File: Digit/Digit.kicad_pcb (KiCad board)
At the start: 2 copper layers, 107 x 213 mm, 106 parts, among them J1 Power In, J2 Power out, J3 Signal in, J4 Signal out, U1 TLC5952, U2 TLC5952, U3 74LS244

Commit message: Minor changes. BOM
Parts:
- J1: value Power In -> DC IN
- J2: value Power out -> DC OUT
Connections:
- net VCC renamed +5VD
- net Vdrive renamed +15V
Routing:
- net Net-(D33-Pad3): track 35.0 -> 33.2 mm
- net Net-(D25-Pad1): track 37.8 -> 37.2 mm

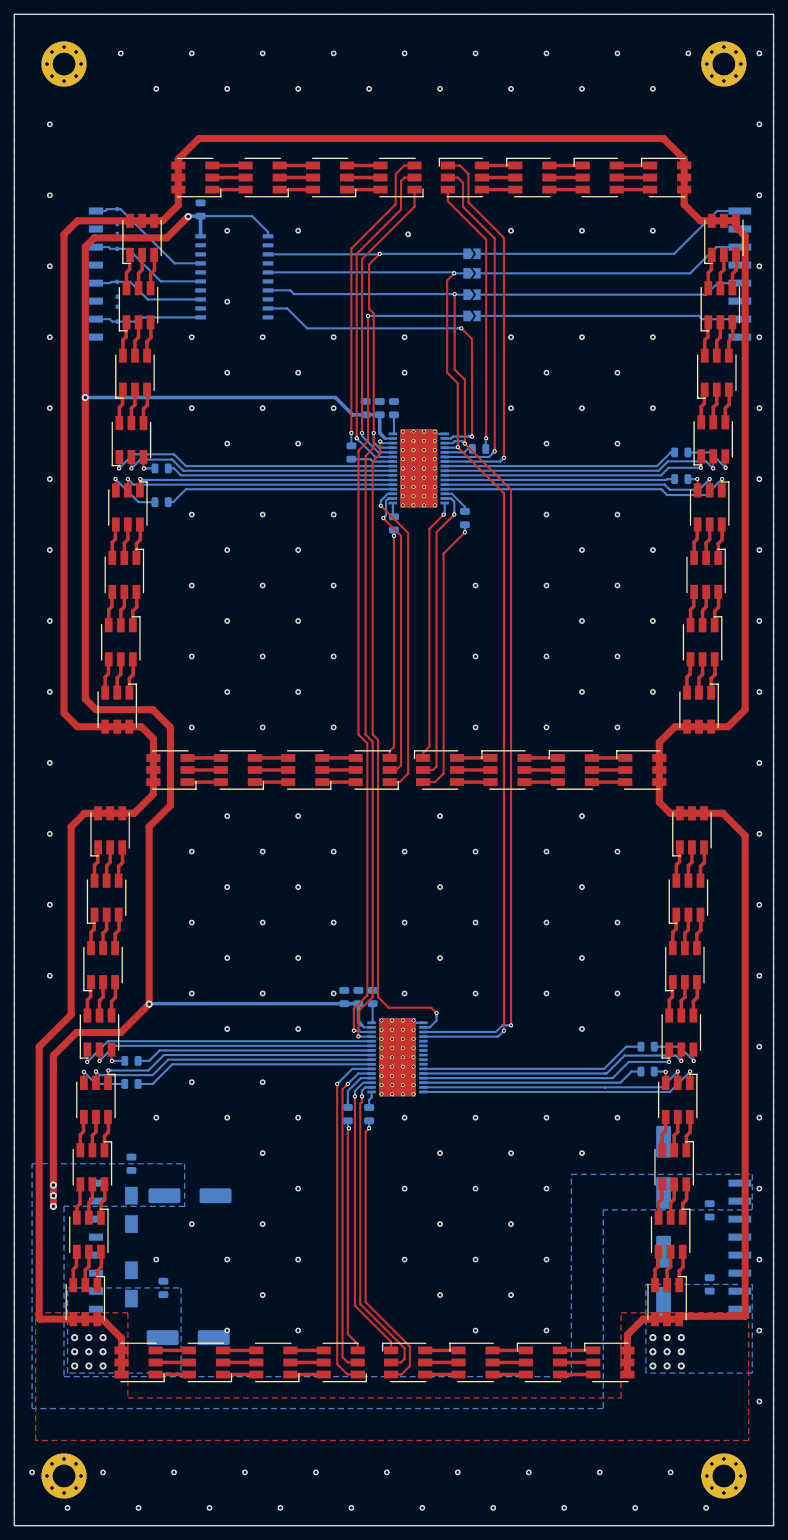
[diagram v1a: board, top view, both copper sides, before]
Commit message: Moved mounting holes. Moved stuff around on controller PCB.
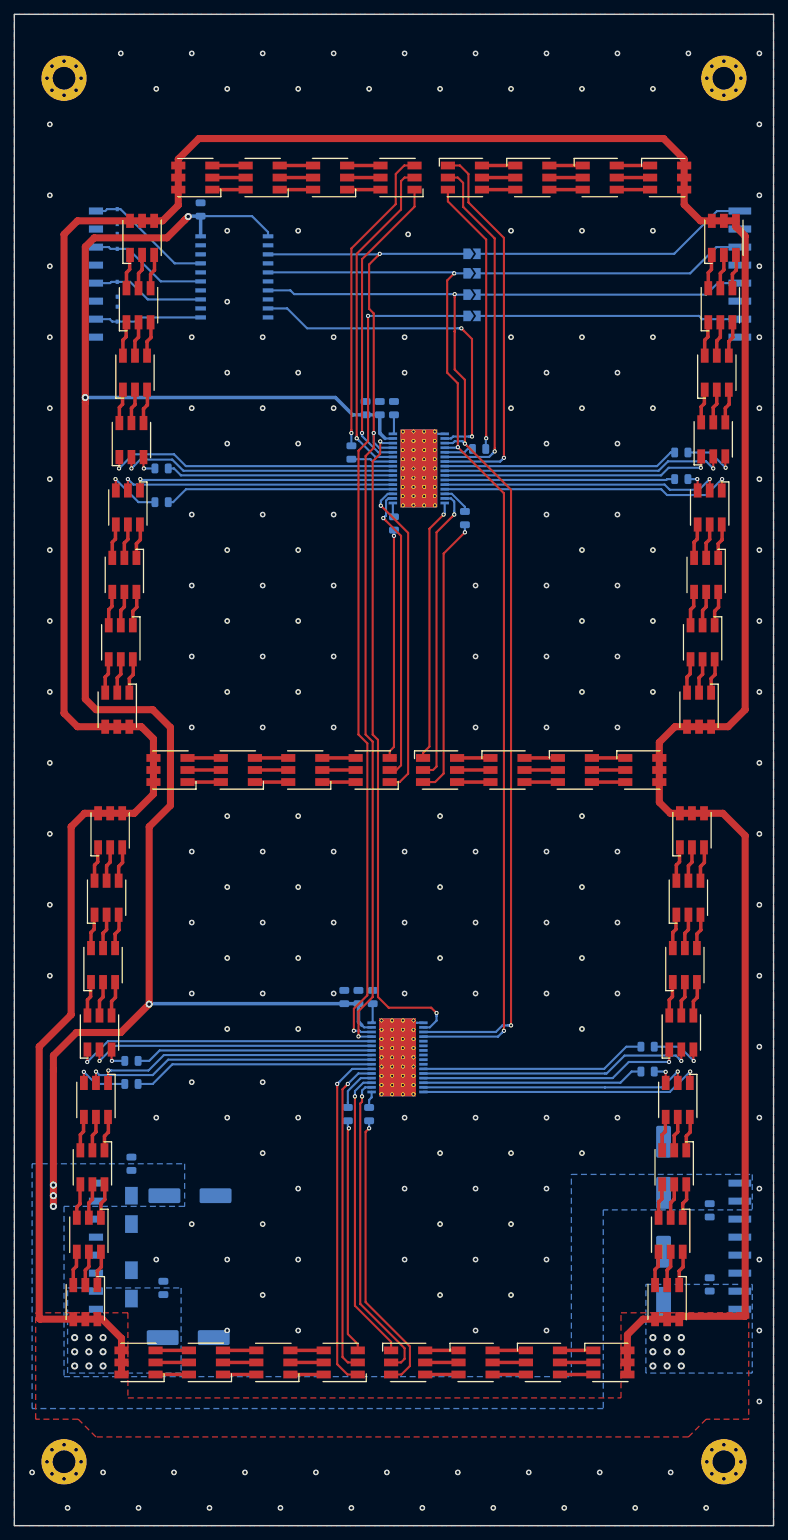
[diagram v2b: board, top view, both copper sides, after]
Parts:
- moved H1 2.00 mm to (69.5, 33.5)
- moved H2 2.00 mm to (69.5, 228.5)
- moved H3 2.00 mm to (162.5, 228.5)
- moved H4 2.00 mm to (162.5, 33.5)
